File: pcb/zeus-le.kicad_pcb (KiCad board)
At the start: 6 copper layers, 50 x 50 mm, 75 parts, among them J1 12402012E212A, J2 S2B-PH-SM4-TB, J3 B5B-PH-SM4-TB, J4 20021121-00010T4LF, J5 Micro_SD_Card_Det1, SW1 EVQPUD02K, U1 TPD6S300ARUKR, U2 RT6160AWSC, U3 MAX20342EWG+, U4 BQ25150YFPT, U5 TLV320ADC6120IRTER, U6 WT02V40V, U7 AP21510FM-7, U8 TPD6F003, U9 LP5810ADSDR

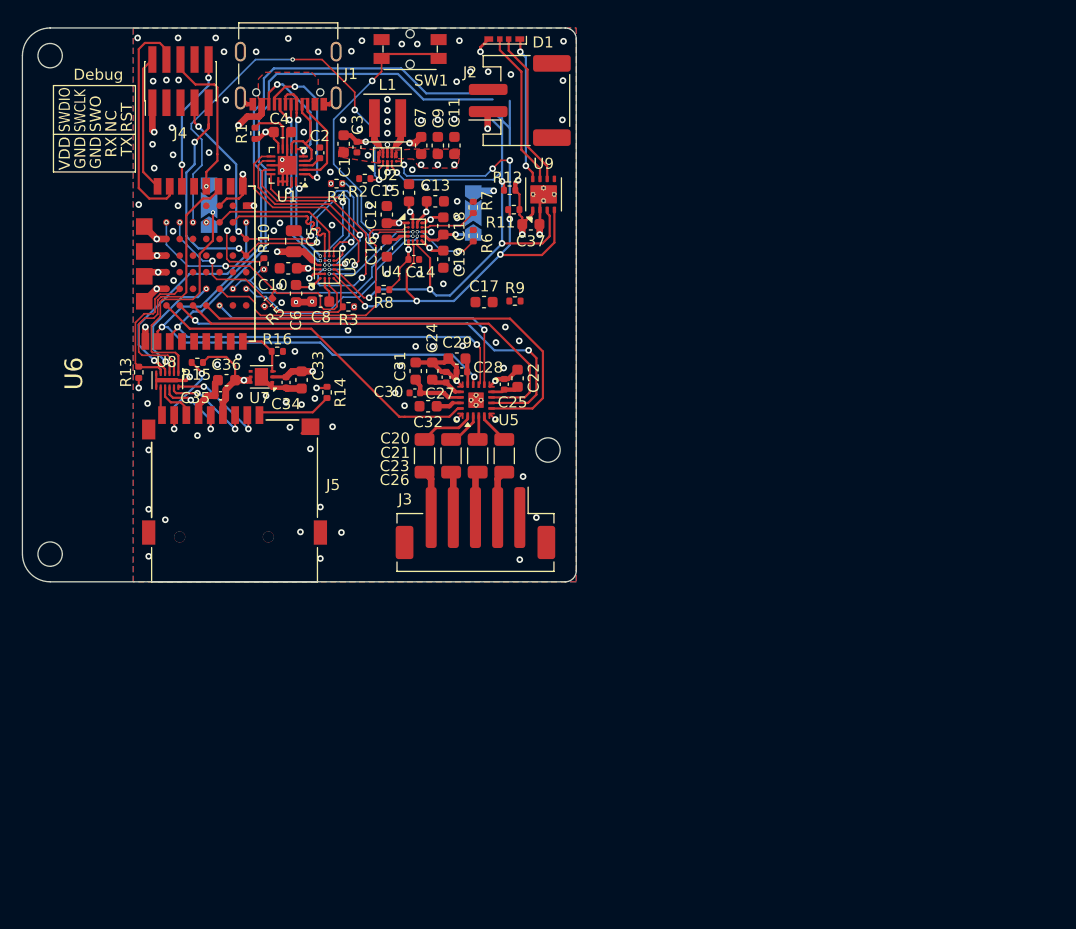
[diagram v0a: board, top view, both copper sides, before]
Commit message: pcb: simplify power supply and define LC filter
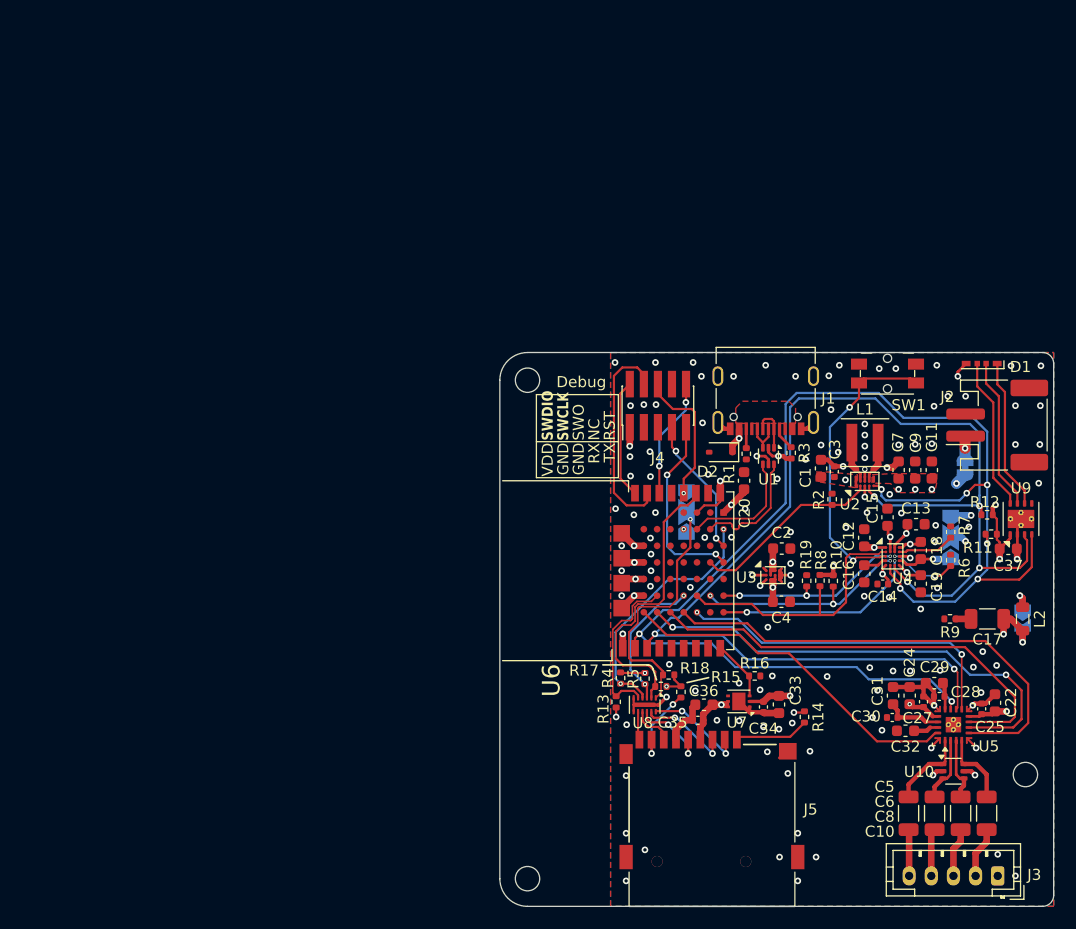
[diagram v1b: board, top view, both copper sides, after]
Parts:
- removed C21, C23, C26: 1µF, Capacitor_SMD:C_1206_3216Metric
- added D2: XCUZ36V, Diode_SMD:D_SOD-323, F.Cu at (156.1, 112.3)
- added JP3: LC Bypass, Jumper:SolderJumper-2_P1.3mm_Open_TrianglePad1.0x1.5mm, B.Cu at (183.3, 127.3)
- added JP4: VBAT, Jumper:SolderJumper-2_P1.3mm_Bridged_RoundedPad1.0x1.5mm, B.Cu at (178.1, 113.7)
- added L2: 22uH, Inductor_SMD:L_0805_2012Metric, F.Cu at (183.3, 127.3)
- added R17: 10k, Resistor_SMD:R_0402_1005Metric, F.Cu at (150.6, 133.4)
- added R18: 10k, Resistor_SMD:R_0402_1005Metric, F.Cu at (151.3, 132.4)
- added R19: 100k, Resistor_SMD:R_0402_1005Metric, F.Cu at (163.8, 123.9)
- added U10: D3V3F4U6S-7, Package_TO_SOT_SMD:SOT-363_SC-70-6, F.Cu at (177.1, 141.1)
- C10, C6, C8: footprint Capacitor_SMD:C_0603_1608Metric -> Capacitor_SMD:C_1206_3216Metric
- C17: value TBD -> 100uF; footprint Capacitor_SMD:C_0603_1608Metric -> Capacitor_SMD:C_1206_3216Metric
- C18, C19: value 2.2µF -> 4.7µF
- C2: value 0.1µF -> 1µF; footprint Capacitor_SMD:C_0402_1005Metric -> Capacitor_SMD:C_0603_1608Metric
- C20: value 1µF -> 4.7µF; footprint Capacitor_SMD:C_1206_3216Metric -> Capacitor_SMD:C_0603_1608Metric
- C5: footprint Capacitor_SMD:C_0805_2012Metric -> Capacitor_SMD:C_1206_3216Metric
- J3: value B5B-PH-SM4-TB -> B5B-PH-K-S; footprint Connector_JST:JST_PH_B5B-PH-SM4-TB_1x05-1MP_P2.00mm_Vertical -> Connector_JST:JST_PH_B5B-PH-K_1x05_P2.00mm_Vertical
- J5: value Micro_SD_Card_Det1 -> MSD-1-A
- R1, R3: value 100k -> 5.1k
- R4, R5: value 100k -> 10k
- R9: value TBD -> 0.1
- U1: value TPD6S300ARUKR -> NUF2042XV6T1G; footprint Package_DFN_QFN:WQFN-20-1EP_3x3mm_P0.4mm_EP1.7x1.7mm -> Package_TO_SOT_SMD:SOT-563
- U3: value MAX20342EWG+ -> KTS1662EUW-TR; footprint zeus-le:Maxim_WLP-24_2.018x2.618mm_Layout6x4_P0.4mm_Ball0.27mm_Pad0.25mm_NSMD -> zeus-le:Kinetic_WLCSP-12_1.94x1.28mm_Layout4x3_P0.4mm_Ball0.25mm_Pad0.25mm_NSMD
- U6: value WT02V40V -> WT02V40V-V2
- U8: value TPD6F003 -> TPD6F003DQDR
- moved C10 80.0 mm to (180.1, 144.9), turned to 90 degrees
- moved C5 75.8 mm to (173.0, 144.9), turned to 90 degrees
- moved C6 74.3 mm to (175.3, 144.9), turned to 90 degrees
- moved C8 74.0 mm to (177.7, 144.9), turned to 90 degrees
- moved C4 61.9 mm to (161.5, 125.8)
- moved R10 58.8 mm to (166.2, 123.9)
- moved J3 56.9 mm to (181.1, 150.6)
- moved C2 54.9 mm to (161.6, 121.0), turned to 0 degrees
- moved C17 53.7 mm to (180.1, 127.3), turned to 180 degrees
- moved R1 53.0 mm to (158.3, 112.4), turned to -90 degrees
- moved R15 52.8 mm to (152.4, 133.9), turned to -90 degrees
- moved R13 52.4 mm to (146.6, 134.8), turned to 90 degrees
- moved C13 52.3 mm to (173.7, 118.8)
- moved C15 52.2 mm to (171.1, 118.2)
- moved C16 52.2 mm to (169.0, 123.3)
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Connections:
- C10 pad 1: VBUS -> Net-(J3-Pin_2)
- C10 pad 2: GND -> /Audio/R-
- C12 pad 1: VBUS -> /Power/VBUS
- C13 pad 1: /Power/VBAT -> Net-(JP4-B)
- C2 pad 1: Net-(U1-VBIAS) -> /Power/VBUS
- C20 pad 1: Net-(J3-Pin_5) -> VBUS_DET
- C20 pad 2: Net-(U5-IN1P) -> GND
- C4 pad 1: VDDD -> /Power/VBUS_RAW
- C5 pad 1: GND -> Net-(J3-Pin_5)
- C5 pad 2: /Power/VBUS_RAW -> /Audio/L+
- C6 pad 1: VSYS -> Net-(J3-Pin_4)
- C6 pad 2: GND -> /Audio/L-
- C8 pad 1: Net-(U3-VDD) -> Net-(J3-Pin_3)
- C8 pad 2: GND -> /Audio/R+
- D1 pad 1: Net-(D1-BK) -> Net-(D1-GK)
- D1 pad 2: Net-(D1-GK) -> Net-(D1-BK)
- J1 pad A8: Net-(J1-SBU1) -> unconnected-(J1-SBU1-PadA8)
- J1 pad B8: Net-(J1-SBU2) -> unconnected-(J1-SBU2-PadB8)
- R1 pad 1: VDDD -> Net-(J1-CC2)
- R1 pad 2: Net-(U1-~{FLT}) -> GND
- R13 pad 1: /MCU/SD_DET -> VDDD
- R13 pad 2: VDDD -> /MCU/SD_DET
- R3 pad 1: VDDD -> Net-(J1-CC1)
- R3 pad 2: /MCU/USB_DBG -> GND
- R4 pad 1: VDDD -> /SD Card/VDDD_SD
- R4 pad 2: Net-(U3-~{CE}) -> /MCU/SD.MISO
- R5 pad 1: VDDD -> /SD Card/VDDD_SD
- R5 pad 2: /MCU/USB_INT -> /MCU/SD.SCK
- U1 pad 1: Net-(J1-SBU1) -> /Power/D-
- U1 pad 2: Net-(J1-SBU2) -> GND
- U1 pad 3: Net-(U1-VBIAS) -> /Power/D+
- U1 pad 4: Net-(J1-CC1) -> /MCU/USB.D+
- U1 pad 5: Net-(J1-CC2) -> unconnected-(U1-VBUS-Pad5)
- U1 pad 6: Net-(J1-CC2) -> /MCU/USB.D-
- U3 pad A1: VSYS -> GND
- U3 pad A2: GND -> /Power/VBUS
- U3 pad A3: VBUS -> /Power/VBUS
- U3 pad A4: /Power/VBUS_RAW -> GND
- U3 pad B1: Net-(U3-VDD) -> VBUS_DET
- U3 pad B2: GND -> /Power/VBUS
- U3 pad B3: Net-(U1-SBU2) -> /Power/VBUS_RAW
- U3 pad B4: Net-(U1-SBU1) -> GND
- U3 pad C1: /MCU/USB_INT -> GND
- U3 pad C2: Net-(U3-~{CE}) -> /Power/VBUS_RAW
- U3 pad C3: Net-(U1-CC2) -> /Power/VBUS_RAW
- U3 pad C4: Net-(U1-CC1) -> GND
- U4 pad A1: VBUS -> /Power/VBUS
- U4 pad A3: /Power/VBAT -> Net-(JP4-B)
- U4 pad B3: /Power/VBAT -> Net-(JP4-B)
- U4 pad C2: Net-(U3-~{CE}) -> /MCU/CHG_EN
- U5 pad 1: Net-(U5-IN1P) -> /Audio/L+
- U5 pad 2: Net-(U5-IN1M) -> /Audio/L-
- U5 pad 3: Net-(U5-IN2P_GPI1) -> /Audio/R+
- U5 pad 4: Net-(U5-IN2M_GPO1) -> /Audio/R-
- U6 pad A6: /MCU/CHG_LP -> /MCU/CHG_EN
- U6 pad C5: unconnected-(U6-P020-PadC5) -> /MCU/VDDD_VSEL
- U6 pad E0: /MCU/USB_INT -> unconnected-(U6-P104-PadE0)
- U6 pad E1: /MCU/USB_DBG -> unconnected-(U6-P105-PadE1)
- U6 pad E2: /MCU/VDDD_VSEL -> unconnected-(U6-P106-PadE2)
- U6 pad F6: VBUS -> VBUS_DET
- U6 pad Z6: unconnected-(U6-P115-PadZ6) -> /MCU/CHG_LP
- U9 pad 6: Net-(D1-BK) -> Net-(D1-RK)
- U9 pad 8: Net-(D1-RK) -> Net-(D1-BK)
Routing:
- net VBUS: track 28.1 -> 0.00 mm, vias 3 -> 0
- net /MCU/USB_INT: track 24.1 -> 0.00 mm, vias 2 -> 0
- net /Audio/I2C.SCL: track 143.2 -> 119.6 mm, vias 7 -> 6
- net Net-(U1-SBU2): track 23.4 -> 0.00 mm, vias 2 -> 0
- net /MCU/USB_DBG: track 22.7 -> 0.00 mm, vias 2 -> 0
- net /MCU/VDDD_VSEL: track 39.5 -> 17.2 mm, vias 4 -> 0
- net /MCU/UART.TX: track 38.7 -> 17.2 mm, vias 4 -> 2
- net /MCU/UART.RX: track 33.6 -> 12.6 mm, vias 4 -> 2
- net Net-(U1-CC2): track 20.3 -> 0.00 mm, vias 2 -> 0
- net Net-(U1-CC1): track 18.6 -> 0.00 mm, vias 2 -> 0
- net /MCU/CHG_EN: track 0.00 -> 17.4 mm, vias 0 -> 3
- net Net-(U3-~{CE}): track 16.8 -> 0.00 mm, vias 3 -> 0
- net /Power/VBUS: track 0.00 -> 16.3 mm, vias 0 -> 2
- net VSYS: track 26.8 -> 11.1 mm, vias 3 -> 2
- net /Power/D+: track 18.8 -> 3.37 mm, vias 3 -> 0
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- removed copper zone on In2.Cu, net GND
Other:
- board text added: "+"
- board text added: "-"
- board text added: "BAT"
- board text added: "Designed by Ben Wolsieffer"
- board text added: "L+"
- board text added: "L-"
- board text added: "LC Bypass"
- board text added: "P0.11/SWO"
- board text added: "P1.07"
- board text added: "R+"
- board text added: "R-"
- board text added: "SD_CS"
- board text added: "VBAT"
- board text added: "VDDA"
- board text added: "VDDA_LDO"
- board text added: "VDDD"
- board text added: "rev 1.0"
- board text added: "zeus-le"

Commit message: pcb: pretty much the final version
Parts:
- added J6: B2B-PH-K-S, Connector_JST:JST_PH_B2B-PH-K_1x02_P2.00mm_Vertical, F.Cu at (182.9, 110.8)
- R11, R12: value TBD -> 1.21k
- R9: footprint Resistor_SMD:R_0402_1005Metric -> Resistor_SMD:R_0603_1608Metric
- U4: value BQ25150YFPT -> BQ25150YFPR; footprint zeus-le:Texas_DSBGA-20_1.615x2.015mm_Layout4x5_P0.4mm -> zeus-le:Texas_DSBGA-20_1.615x2.015mm_Layout4x5_P0.4mm_NSMD
- U6: value WT02V40V-V2 -> WT02C40C-V3; footprint zeus-le:WT02V40V -> zeus-le:WT02C40C
- moved R9 0.47 mm to (176.3, 127.3)
- moved C32 0.20 mm to (172.7, 137.7)
- moved H2 0.11 mm to (183.6, 141.3)
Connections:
- U6 pad A4: /MCU/CHG_PG -> unconnected-(U6-P016-PadA4)
- U6 pad Z5: unconnected-(U6-P114-PadZ5) -> /MCU/CHG_PG
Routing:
- net /Power/VBAT: track 2.22 -> 7.48 mm
- net GND: track 61.6 -> 57.6 mm, vias 127 -> 123
- net /Power/VBUS_RAW: track 23.3 -> 21.5 mm, vias 3 -> 2
- net /MCU/CHG_PG: track 25.1 -> 23.9 mm
- net VSYS: track 11.1 -> 11.8 mm
- net VDDD: track 44.7 -> 45.2 mm
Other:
- outline, holes or cut-outs redrawn

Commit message: pcb: use debug connector with shroud
This also gets the connector up higher so the cable won't hit the USB
connector as much.
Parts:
- J4: value 20021121-00010T4LF -> BD125-10-A-0305-0580-L-B
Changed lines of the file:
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@@
 			)
 		)
-		(property "Value" "20021121-00010T4LF"
+		(property "Value" "BD125-10-A-0305-0580-L-B"
 			(at 0 4.235 -90)
 			(layer "F.Fab")
@@
 			)
 		)
-		(property "Description" "Generic connector, double row, 02x05, odd/even pin numbering scheme (row 1 odd numbers, row 2 even numbers), script generated (kicad-library-utils/schlib/autogen/connector/)"
+		(property "Description" "Connector Header Surface Mount 10 position 0.050\" (1.27mm)"
 			(at 0 0 90)
 			(unlocked yes)
@@
 			(pintype "passive")
 		)
-		(model "${KICAD8_3DMODEL_DIR}/Connector_PinHeader_1.27mm.3dshapes/PinHeader_2x05_P1.27mm_Vertical_SMD.wrl"
+		(model "${KIPRJMOD}/zeus-le.3dshapes/GCT_BD125-10-A-0305-0580-L-B.step"
 			(offset
 				(xyz 0 0 0)
@@
 			)
 			(rotate
-				(xyz 0 0 0)
-			)
-		)
+				(xyz -90 0 90)
+			)
+		)

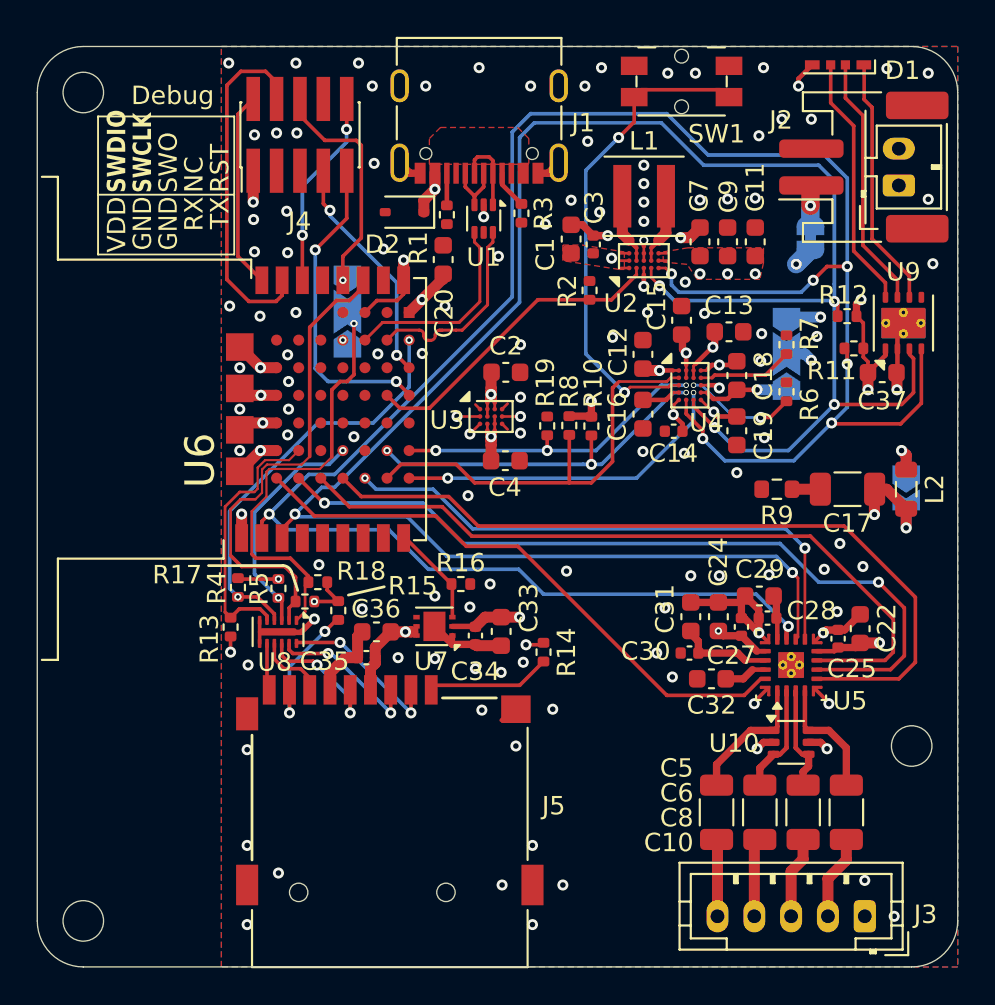
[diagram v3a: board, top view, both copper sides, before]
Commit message: pcb: rotate debug connector
This prevents it from interfering with the USB connector.
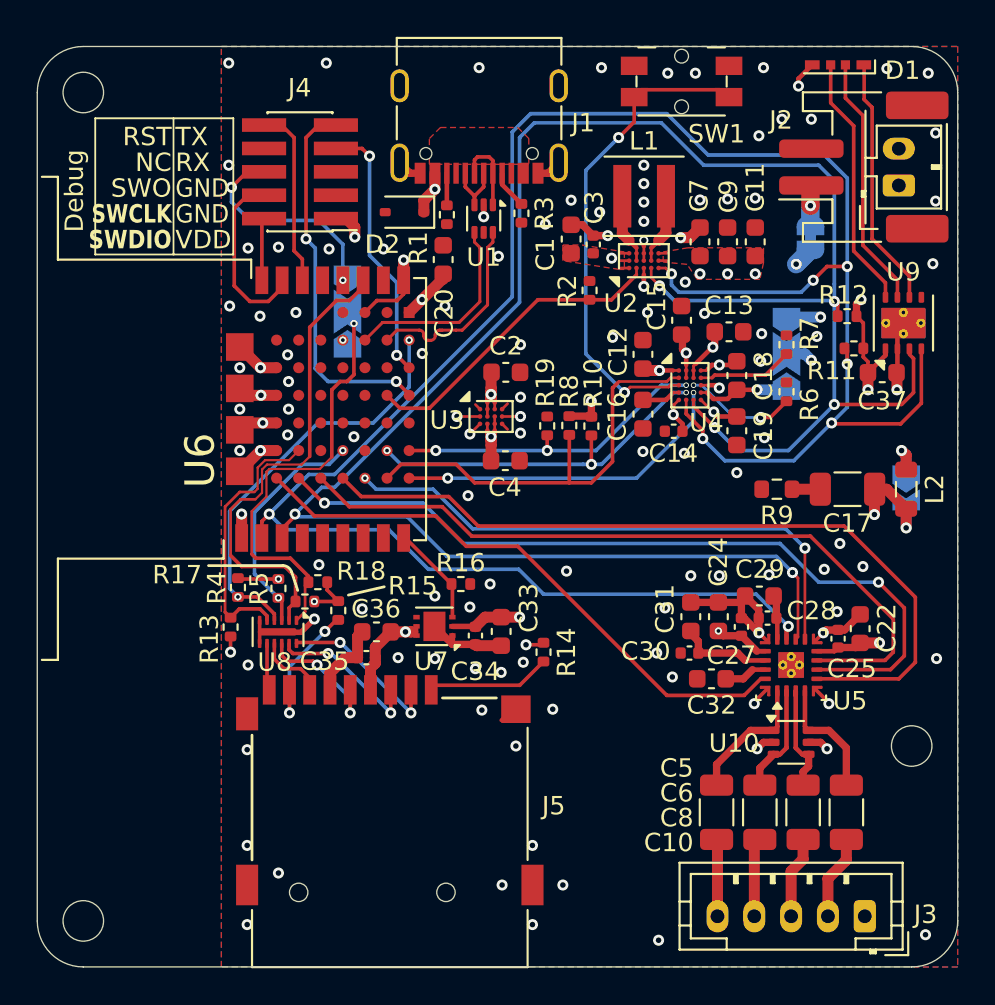
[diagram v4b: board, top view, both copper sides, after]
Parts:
- moved J4 2.01 mm to (150.4, 110.1), turned to 180 degrees
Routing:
- net /MCU/SWCLK: track 19.2 -> 9.78 mm
- net /MCU/SWDIO: track 10.7 -> 3.40 mm
- net /MCU/UART.TX: track 17.2 -> 20.4 mm
- net /MCU/UART.RX: track 12.6 -> 14.4 mm
- net /MCU/RST: track 10.8 -> 9.85 mm, vias 2 -> 0
- net unconnected-(J4-Pin_8-Pad8): track 0.00 -> 0.83 mm
- net /MCU/SWO: track 12.8 -> 12.1 mm, vias 1 -> 2
- net GND: vias 123 -> 115
- net VDDD: vias 17 -> 16
